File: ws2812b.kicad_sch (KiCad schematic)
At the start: 19 parts, among them J22 WS2812, U10 74LVC1G17, U9 74LVC1G17

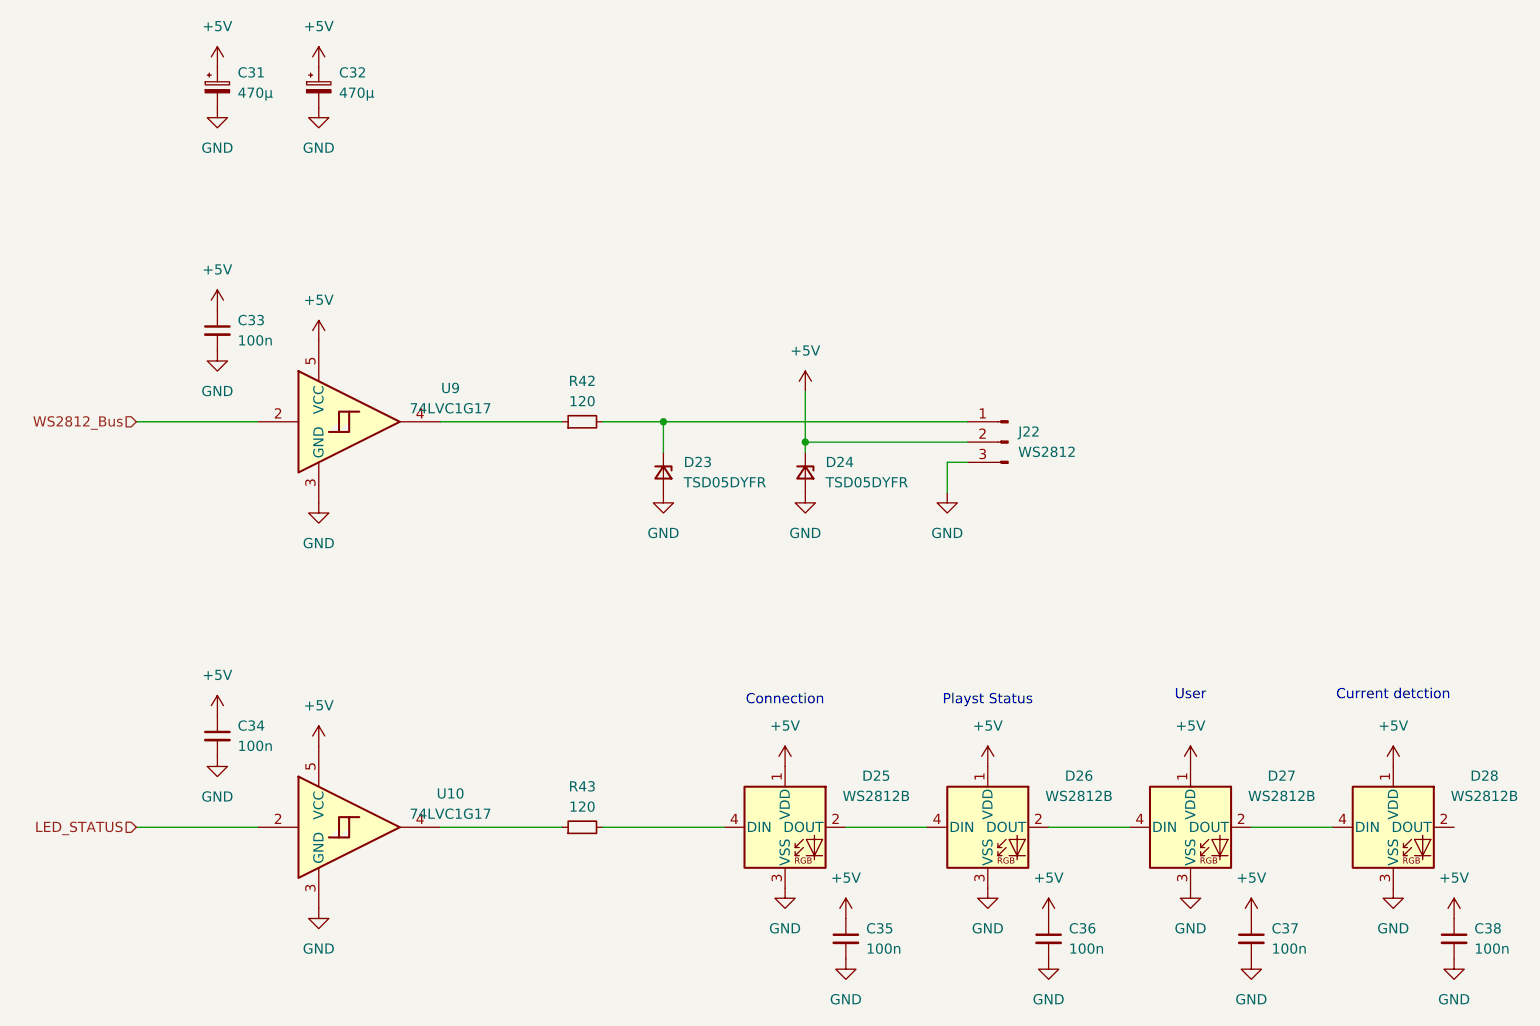
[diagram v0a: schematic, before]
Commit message: - I2C entfernt - Logo hinzugefügt - Spannungsauswahl für Audio (USB oder +5V) hinzugefügt - Spannung für WS2812 LEDs ändert sich jetzt zusammen mit +5VD Auswahl
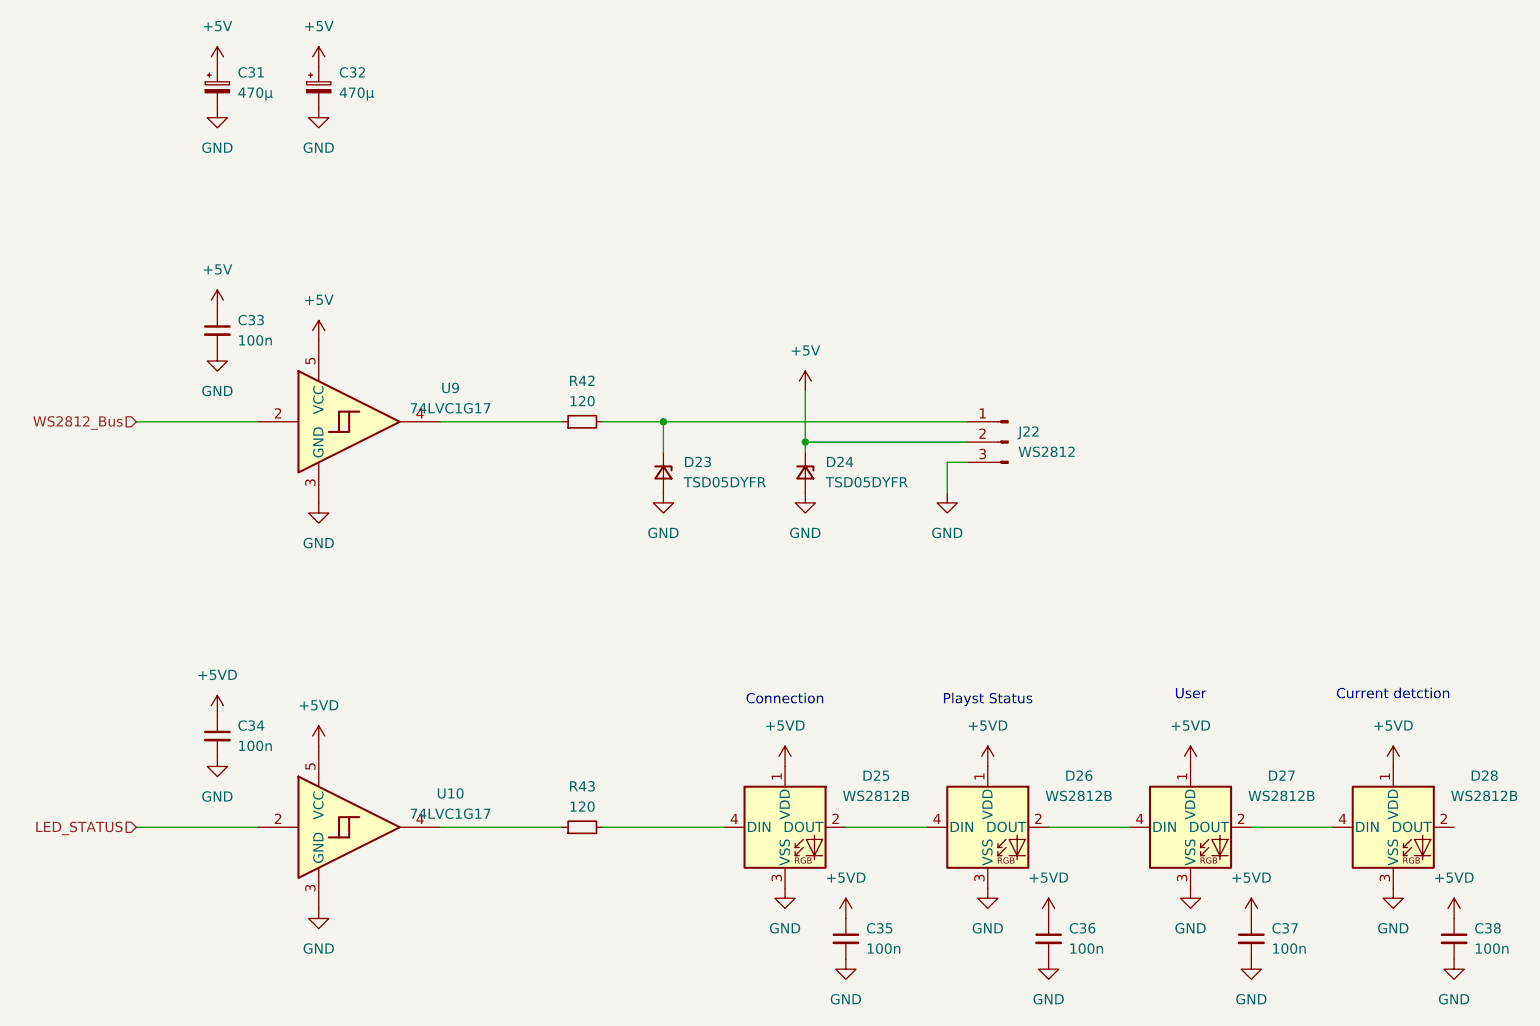
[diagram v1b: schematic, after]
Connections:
- net +5V: no longer C34.1, C35.1, C36.1, C37.1, C38.1, D25.1 (VDD), D26.1 (VDD), D27.1 (VDD), D28.1 (VDD), U10.5 (VCC)
- new net +5VD: C34.1, C35.1, C36.1, C37.1, C38.1, D25.1 (VDD), D26.1 (VDD), D27.1 (VDD), D28.1 (VDD), U10.5 (VCC)

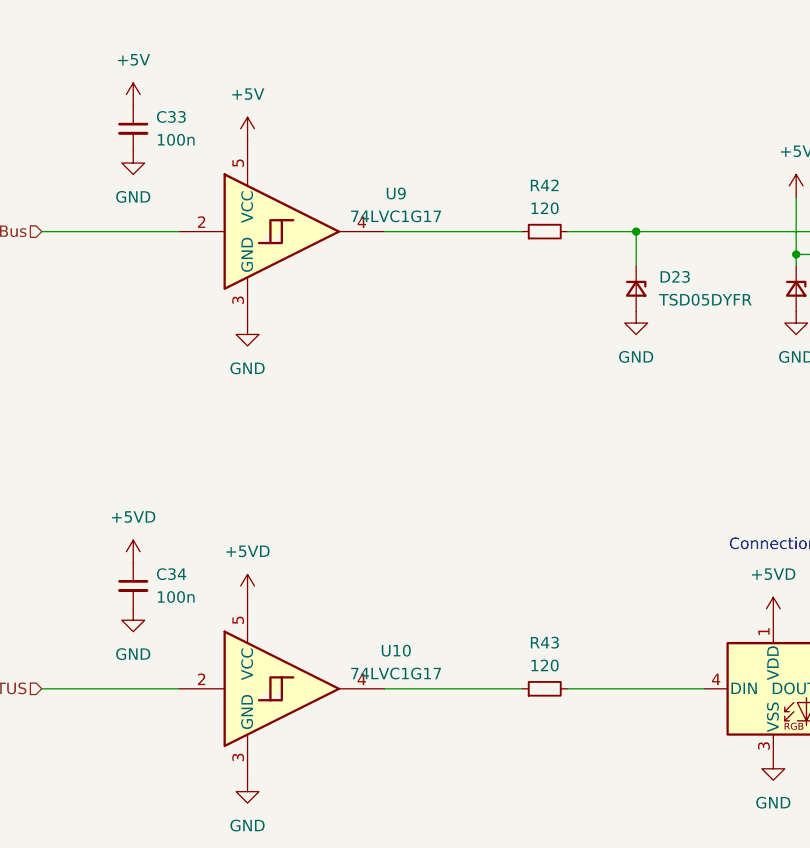
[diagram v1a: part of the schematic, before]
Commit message: Changed the WS2812 driver IC Optimized the Analog GND and AVCC routing Changed RS485 driver Removed TVS Diode at the RS485 driver (already has 15kV rating)
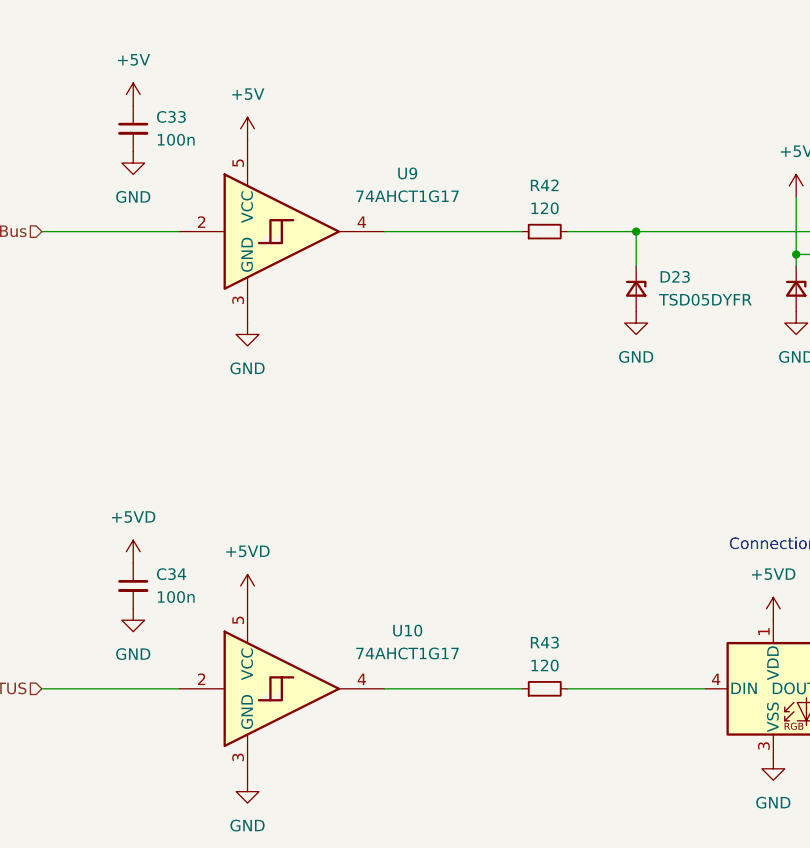
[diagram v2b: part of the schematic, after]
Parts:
- U10, U9: value 74LVC1G17 -> 74AHCT1G17
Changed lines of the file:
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@@
 		(fields_autoplaced yes)
 		(property "Reference" "U10"
-			(at 105.41 122.8091 0)
-			(effects
-				(font
-					(size 1.27 1.27)
-				)
-			)
-		)
-		(property "Value" "74LVC1G17"
-			(at 105.41 125.3491 0)
+			(at 106.68 120.5798 0)
+			(effects
+				(font
+					(size 1.27 1.27)
+				)
+			)
+		)
+		(property "Value" "74AHCT1G17"
+			(at 106.68 123.1198 0)
 			(effects
 				(font
@@
 		(fields_autoplaced yes)
 		(property "Reference" "U9"
-			(at 105.41 72.0091 0)
-			(effects
-				(font
-					(size 1.27 1.27)
-				)
-			)
-		)
-		(property "Value" "74LVC1G17"
-			(at 105.41 74.5491 0)
-			(effects
-				(font
+			(at 106.68 69.7798 0)
+			(effects
+				(font
+					(size 1.27 1.27)
+				)
+			)
+		)
+		(property "Value" "74AHCT1G17"
+			(at 106.68 72.3198 0)
+			(effects
+				(font

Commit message: Footprint changes
Changed WS2812 from 5050 to 2020
Changed ESP32 to correct revision
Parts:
- D25, D26, D27, D28: footprint LED_SMD:LED_WS2812B_PLCC4_5.0x5.0mm_P3.2mm -> LED_SMD:LED_WS2812B-2020_PLCC4_2.0x2.0mm
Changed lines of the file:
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@@
 			)
 		)
-		(property "Footprint" "LED_SMD:LED_WS2812B_PLCC4_5.0x5.0mm_P3.2mm"
+		(property "Footprint" "LED_SMD:LED_WS2812B-2020_PLCC4_2.0x2.0mm"
 			(at 199.39 134.62 0)
 			(effects
@@
 			)
 		)
-		(property "Footprint" "LED_SMD:LED_WS2812B_PLCC4_5.0x5.0mm_P3.2mm"
+		(property "Footprint" "LED_SMD:LED_WS2812B-2020_PLCC4_2.0x2.0mm"
 			(at 173.99 134.62 0)
 			(effects
@@
 			)
 		)
-		(property "Footprint" "LED_SMD:LED_WS2812B_PLCC4_5.0x5.0mm_P3.2mm"
+		(property "Footprint" "LED_SMD:LED_WS2812B-2020_PLCC4_2.0x2.0mm"
 			(at 148.59 134.62 0)
 			(effects
@@
 			)
 		)
-		(property "Footprint" "LED_SMD:LED_WS2812B_PLCC4_5.0x5.0mm_P3.2mm"
+		(property "Footprint" "LED_SMD:LED_WS2812B-2020_PLCC4_2.0x2.0mm"
 			(at 224.79 134.62 0)
 			(effects
